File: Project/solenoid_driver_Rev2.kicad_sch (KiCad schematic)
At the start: 211 parts, among them Q1 PMGD780SN, Q2 PMGD780SN, Q3 PMGD780SN, Q4 PMGD780SN, Q5 PMGD780SN, Q6 PMGD780SN, Q7 PMGD780SN, Q8 PMGD780SN, U10 NCV272DMR2G, U11 NCV272DMR2G, U12 NCV272DMR2G, U13 NCV272DMR2G, U14 NCV272DMR2G, U15 NCV272DMR2G, U16 NCV272DMR2G, U25 INA199xxDCK, U9 NCV272DMR2G

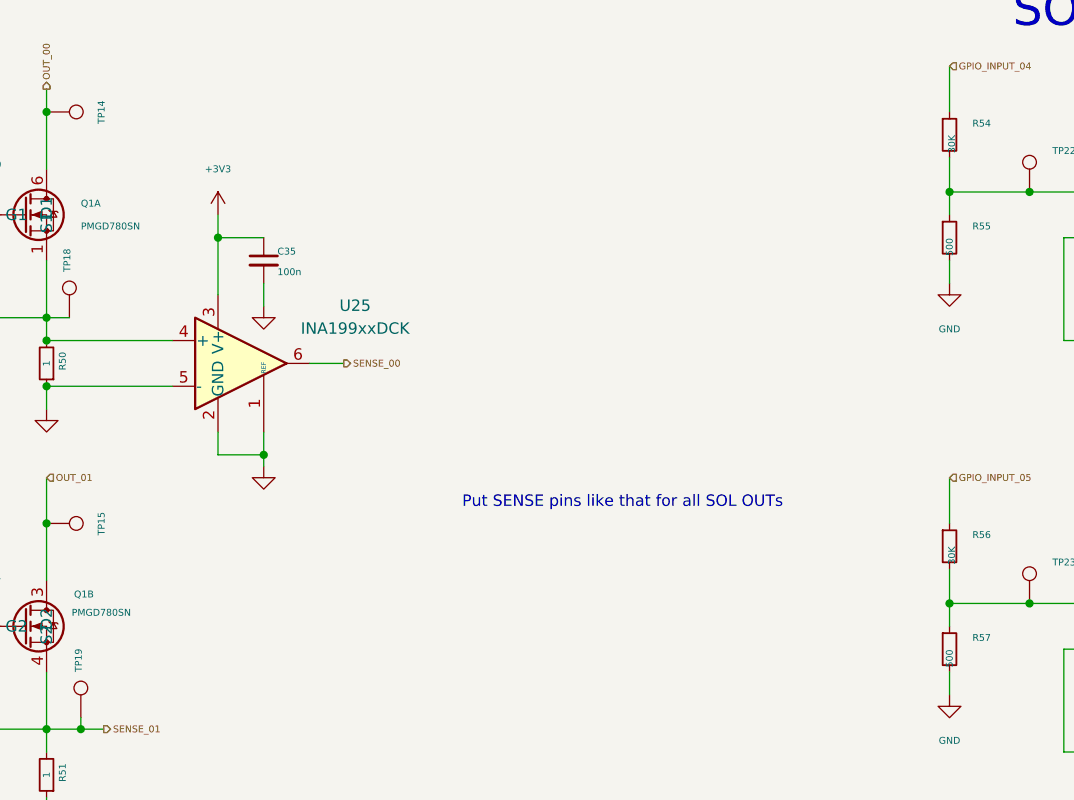
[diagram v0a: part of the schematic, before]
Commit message: FINISHED TODO LIST and updated current sense
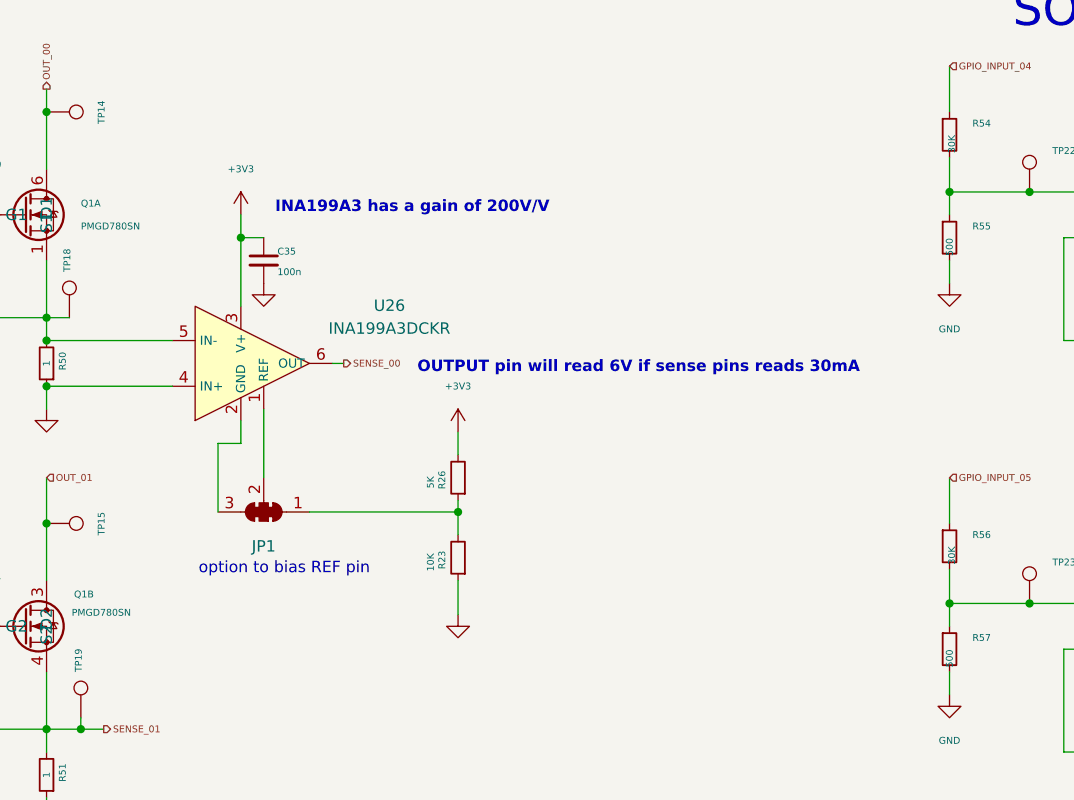
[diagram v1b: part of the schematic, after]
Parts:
- removed U25: INA199xxDCK, Package_TO_SOT_SMD:SOT-363_SC-70-6, symbol Amplifier_Current:INA199xxDCK
- added JP1: SolderJumper_3_Bridged123, symbol Jumper:SolderJumper_3_Bridged123
- added R23: 10K, Resistor_SMD:R_0603_1608Metric, symbol Device:R_Small
- added R26: 5K, Resistor_SMD:R_0603_1608Metric, symbol Device:R_Small
- added U26: INA199A3DCKR, project_footprints:INA199A3DCKR, symbol Project_Symbols:INA199A3DCKR
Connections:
- net +3V3: now also R26.2, U26.3 (V+)
- net GND: now also R23.1, U26.4 (IN+)
- net SENSE_00: now also U26.6 (OUT)
- net at Q1.1 (S1), R38.2, R50.2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: now also U26.5 (IN-)
- new net: JP1.1 (A), R23.2, R26.1
- new net: JP1.2 (C), U26.1 (REF)
- new net: JP1.3 (B), U26.2 (GND)
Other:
- note added: "INA199A3 has a gain of 200V/V"
- note added: "OUTPUT pin will read 6V if sense pins reads 30mA"
- note added: "option to bias REF pin"
- note removed: "Put SENSE pins like that for all SOL OUTs"

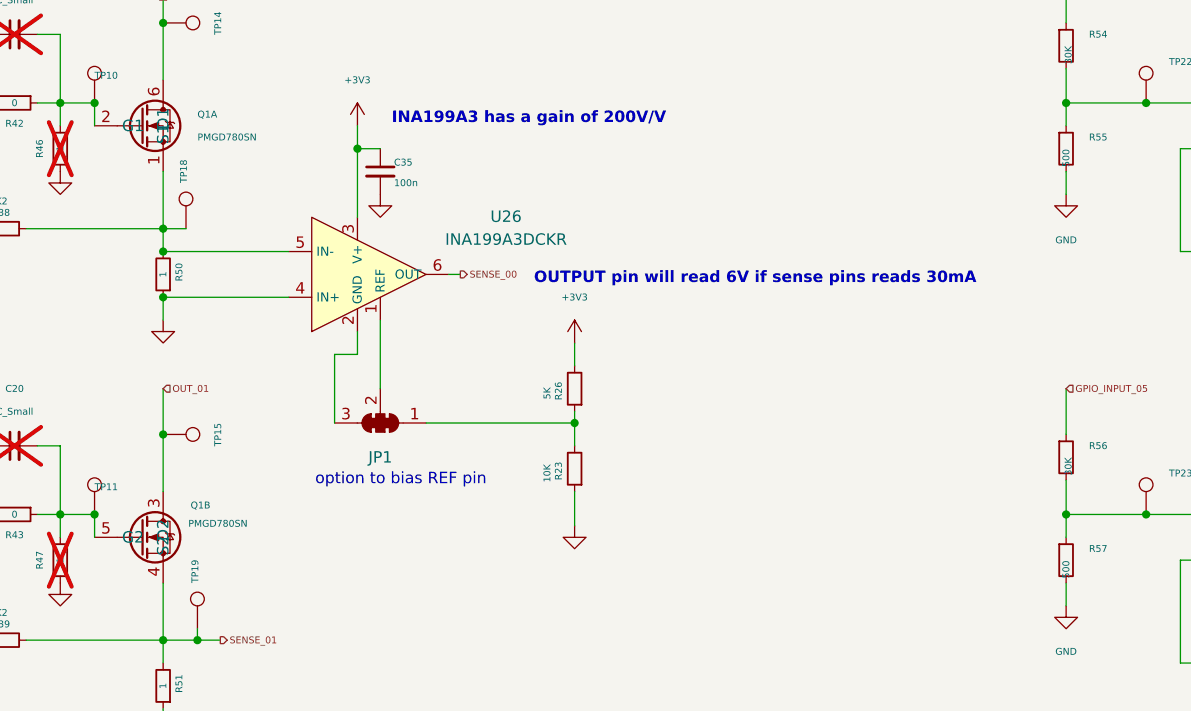
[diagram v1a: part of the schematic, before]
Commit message: Comparator Circuit idea
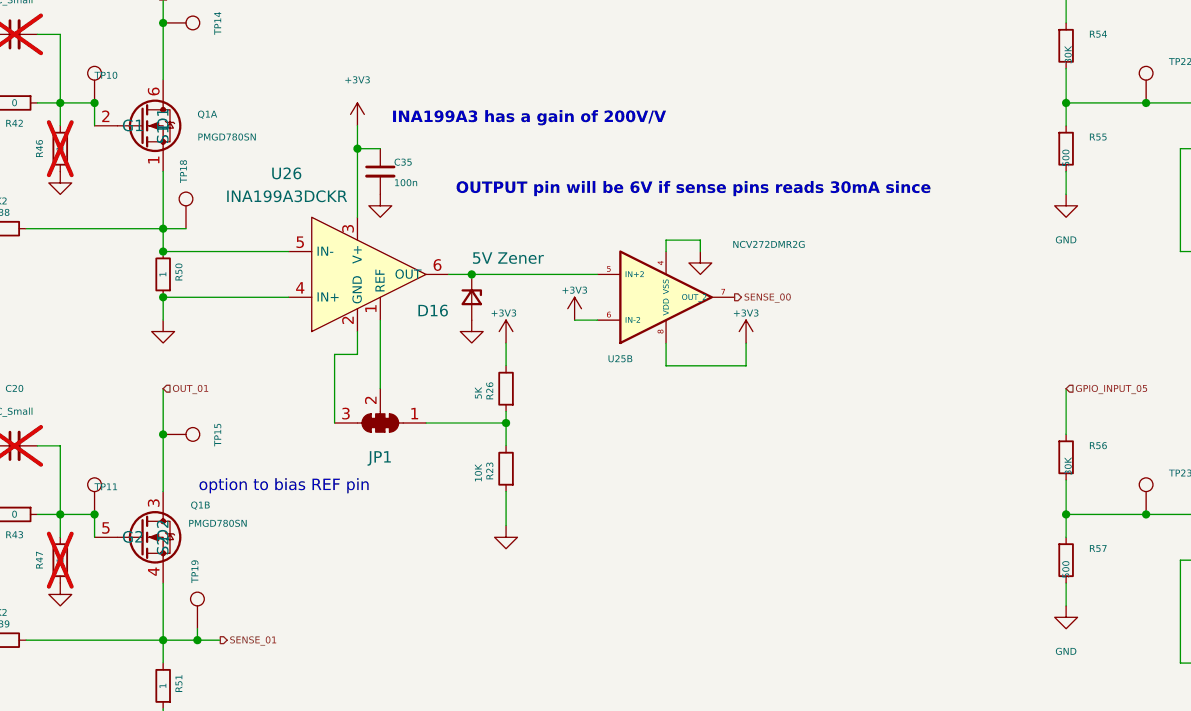
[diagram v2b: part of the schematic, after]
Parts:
- added D16: 5V Zener, symbol Device:D_Zener_Small
- added U25: NCV272DMR2G, Package_SO:MSOP-8_3x3mm_P0.65mm, symbol Project_Symbols:OpAmp_NCV272
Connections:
- net +3V3: now also U25.6 (IN-2), U25.8 (VDD)
- net GND: now also D16.2 (A), U25.4 (VSS)
- net SENSE_00: now also U25.7 (OUT_2); no longer U26.6 (OUT)
- new net: D16.1 (K), U25.5 (IN+2), U26.6 (OUT)
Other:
- note added: "OUTPUT pin will be 6V if sense pins reads 30mA since"
- note removed: "OUTPUT pin will read 6V if sense pins reads 30mA"
- moved on the sheet: R23, R26

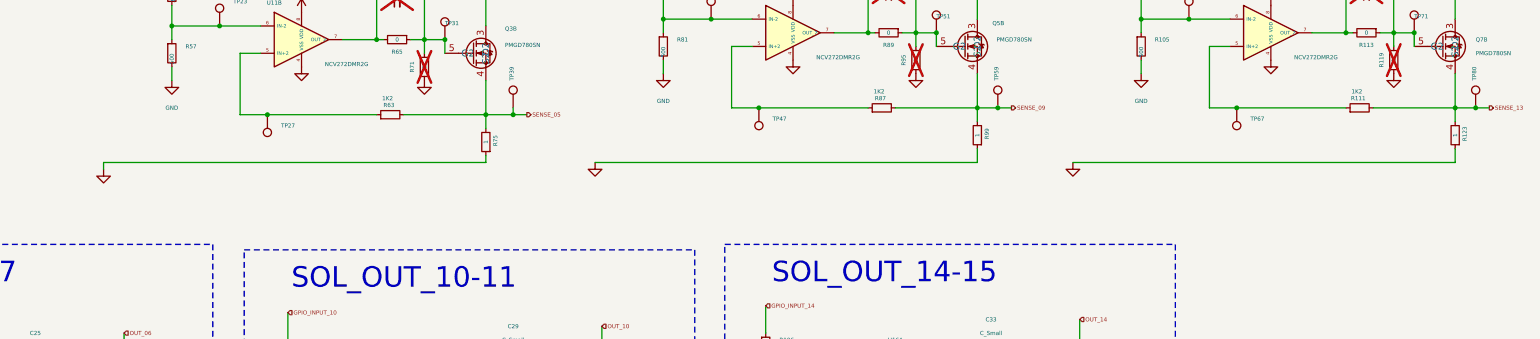
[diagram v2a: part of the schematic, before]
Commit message: finished schematic and footprint assignments
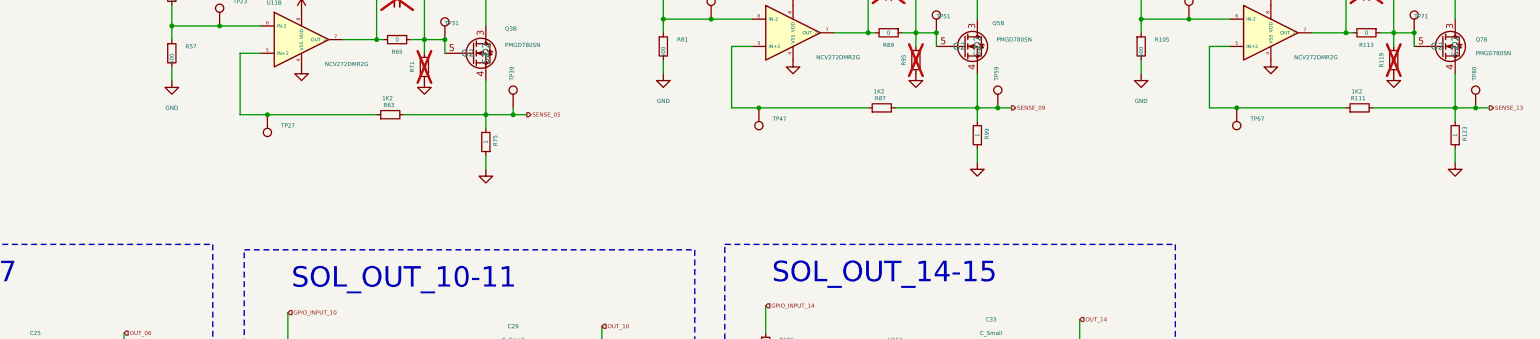
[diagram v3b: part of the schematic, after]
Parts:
- D16: footprint (none) -> Resistor_SMD:R_0603_1608Metric
- JP1: footprint (none) -> Jumper:SolderJumper-3_P1.3mm_Open_Pad1.0x1.5mm
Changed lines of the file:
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@@
 	(wire
 		(pts
-			(xy 427.99 119.38) (xy 356.87 119.38)
-		)
-		(stroke
-			(width 0)
-			(type default)
-		)
-	)
-	(wire
-		(pts
 			(xy 166.37 157.48) (xy 168.91 157.48)
 		)
@@
 	(wire
 		(pts
-			(xy 247.65 119.38) (xy 176.53 119.38)
-		)
-		(stroke
-			(width 0)
-			(type default)
-		)
-	)
-	(wire
-		(pts
 			(xy 261.62 166.37) (xy 261.62 163.83)
 		)
@@
 	(wire
 		(pts
-			(xy 176.53 119.38) (xy 176.53 120.65)
-		)
-		(stroke
-			(width 0)
-			(type default)
-		)
-	)
-	(wire
-		(pts
 			(xy 369.57 54.61) (xy 369.57 57.15)
 		)
@@
 	(wire
 		(pts
-			(xy 339.09 119.38) (xy 267.97 119.38)
-		)
-		(stroke
-			(width 0)
-			(type default)
-		)
-	)
-	(wire
-		(pts
 			(xy 360.68 176.53) (xy 363.22 176.53)
 		)
@@
 	(wire
 		(pts
-			(xy 247.65 118.11) (xy 247.65 119.38)
+			(xy 247.65 118.11) (xy 247.65 120.65)
 		)
 		(stroke
@@
 			)
 		)
-		(property "Footprint" ""
+		(property "Footprint" "Resistor_SMD:R_0603_1608Metric"
 			(at 123.19 69.85 90)
 			(effects
@@
 			)
 		)
-		(property "Footprint" ""
+		(property "Footprint" "Jumper:SolderJumper-3_P1.3mm_Open_Pad1.0x1.5mm"
 			(at 113.03 83.82 0)
 			(effects
@@
 	(symbol
 		(lib_id "power:GND")
-		(at 356.87 119.38 0)
+		(at 427.99 119.38 0)
 		(unit 1)
 		(exclude_from_sim no)
@@
 		(fields_autoplaced yes)
 		(property "Reference" "#PWR0122"
-			(at 356.87 125.73 0)
+			(at 427.99 125.73 0)
 			(effects
 				(font
@@
 		)
 		(property "Value" "GND"
-			(at 356.87 124.46 0)
+			(at 427.99 124.46 0)
 			(effects
 				(font
@@
 		)
 		(property "Footprint" ""
-			(at 356.87 119.38 0)
+			(at 427.99 119.38 0)
 			(effects
 				(font
@@
 		)
 		(property "Datasheet" ""
-			(at 356.87 119.38 0)
+			(at 427.99 119.38 0)
 			(effects
 				(font
@@
 		)
 		(property "Description" "Power symbol creates a global label with name \"GND\" , ground"
-			(at 356.87 119.38 0)
+			(at 427.99 119.38 0)
 			(effects
 				(font
@@
 	(symbol
 		(lib_id "power:GND")
-		(at 267.97 119.38 0)
+		(at 339.09 119.38 0)
 		(unit 1)
 		(exclude_from_sim no)
@@
 		(fields_autoplaced yes)
 		(property "Reference" "#PWR0106"
-			(at 267.97 125.73 0)
+			(at 339.09 125.73 0)
 			(effects
 				(font
@@
 		)
 		(property "Value" "GND"
-			(at 267.97 124.46 0)
+			(at 339.09 124.46 0)
 			(effects
 				(font
@@
 		)
 		(property "Footprint" ""
-			(at 267.97 119.38 0)
+			(at 339.09 119.38 0)
 			(effects
 				(font
@@
 		)
 		(property "Datasheet" ""
-			(at 267.97 119.38 0)
+			(at 339.09 119.38 0)
 			(effects
 				(font
@@
 		)
 		(property "Description" "Power symbol creates a global label with name \"GND\" , ground"
-			(at 267.97 119.38 0)
+			(at 339.09 119.38 0)
 			(effects
 				(font
@@
 	(symbol
 		(lib_id "power:GND")
-		(at 176.53 120.65 0)
+		(at 247.65 120.65 0)
 		(unit 1)
 		(exclude_from_sim no)
@@
 		(fields_autoplaced yes)
 		(property "Reference" "#PWR090"
-			(at 176.53 127 0)
+			(at 247.65 127 0)
 			(effects
 				(font
@@
 		)
 		(property "Value" "GND"
-			(at 176.53 125.73 0)
+			(at 247.65 125.73 0)
 			(effects
 				(font
@@
 		)
 		(property "Footprint" ""
-			(at 176.53 120.65 0)
+			(at 247.65 120.65 0)
 			(effects
 				(font
@@
 		)
 		(property "Datasheet" ""
-			(at 176.53 120.65 0)
+			(at 247.65 120.65 0)
 			(effects
 				(font
@@
 		)
 		(property "Description" "Power symbol creates a global label with name \"GND\" , ground"
-			(at 176.53 120.65 0)
+			(at 247.65 120.65 0)
 			(effects
 				(font
